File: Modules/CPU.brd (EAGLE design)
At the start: 132.1 x 55.5 mm, 89 parts, among them IC4 93LC66SM, IC5 MIC2026-1YM, J1 USB_A_SMT_FEMALE, J2 USB_A_SMT_FEMALE, J4 SD_CARD_SOCKET, Q1 DMG1012T-7, Q2 DMG1012T-7, Q3 DMG1012T-7, U5 LAN9512-JZX, U6 FSUSB42UMX, Y2 25MHz

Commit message: Added Connectors and Molex
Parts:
- added C1, C2: 0.1uF, SparkFun-Capacitors:0402
- added IC8: AP2331W-7, SamacSys_Parts:SOT95P285X130-3N
- moved R1 67.6 mm to (148.6, 14.0)
- moved PWR_LED 67.6 mm to (144.8, 14.0)
- moved CAM1 56.4 mm to (86.4, 52.1), turned to 180 degrees
- moved SJ4 41.5 mm to (81.3, 41.9)
- moved SJ5 41.0 mm to (74.9, 40.6)
- moved SJ3 39.9 mm to (81.3, 36.8)
- moved CPU1 6.35 mm to (87.6, 8.89)
- moved R22 5.08 mm to (64.0, 17.7)
- moved R23 5.08 mm to (65.4, 17.7)
- moved R24 5.08 mm to (83.7, 17.9)
- moved R25 5.08 mm to (85.1, 17.9)
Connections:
- new net H5V: C2.1, IC8.2
- net 5V: now also C1.2, IC8.3
- net GND: now also C1.1, C2.2, IC8.1
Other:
- board size 132.1 x 55.5 mm -> 132.1 x 55.9 mm

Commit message: Merged HDMI
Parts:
- added IC1: ESD5384NCTBG, SamacSys_Parts:BGA9C40P3X3_114X114X63
- added Q4, Q5: DMG1012T-7, SamacSys_Parts:SOT50P160X80-3N
- added R2: 100K, SparkFun-Resistors:0402
- added U$6: HDMI-A, connectors:HDMI_A
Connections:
- new net HDMI_CEC: CPU1.171, Q4.2
- new net HDMI_CK_N: CPU1.111, U$6.P$12
- new net HDMI_CK_P: CPU1.113, U$6.P$10
- new net HDMI_D0_N: CPU1.117, U$6.P$9
- new net HDMI_D0_P: CPU1.119, U$6.P$7
- new net HDMI_D1_N: CPU1.123, U$6.P$6
- new net HDMI_D1_P: CPU1.125, U$6.P$4
- new net HDMI_D2_N: CPU1.129, U$6.P$3
- new net HDMI_D2_P: CPU1.131, U$6.P$1
- new net HDMI_HPD_N_1V8: CPU1.88, Q5.3, R2.2
- new net HDMI_SCL: CPU1.175, IC1.B3, U$6.P$16
- new net HDMI_SDA: CPU1.173, IC1.A3, U$6.P$15
- new net N$6: IC1.C3, Q5.1, U$6.P$19
- new net N$9: IC1.A2, Q4.3, U$6.P$13
- net 1.8V: now also R2.1
- net GND: now also IC1.B2, IC1.C2, Q5.2, U$6.P$11, U$6.P$17, U$6.P$2, U$6.P$5, U$6.P$8
- net H5V: now also IC1.A1, IC1.C1, Q4.1, U$6.P$18

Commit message: Work
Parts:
- added SJ10: (no value), jumper:SJ
- moved Q4 172.3 mm to (67.3, 44.5)
- moved R2 165.6 mm to (57.1, 43.2)
- moved Q5 165.4 mm to (61.0, 39.4)
- moved IC1 162.6 mm to (62.2, 44.5)
- moved U$6 160.9 mm to (59.7, 50.8), turned to 180 degrees
- moved C2 154.6 mm to (54.6, 44.5)
- moved C1 151.1 mm to (49.5, 36.8)
- moved IC8 147.8 mm to (49.5, 41.9)
- moved C13 129.8 mm to (38.1, 85.1)
- moved C18 115.6 mm to (14.0, 29.2)
- moved FB1 109.6 mm to (14.0, 34.3)
- moved C12 105.4 mm to (-2.54, 30.5)
- moved C11 87.3 mm to (12.7, 64.8)
- moved C16 87.3 mm to (8.89, 64.8)
- moved C17 87.3 mm to (5.08, 64.8)
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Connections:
- net HDMI_CEC: now also SJ10.2

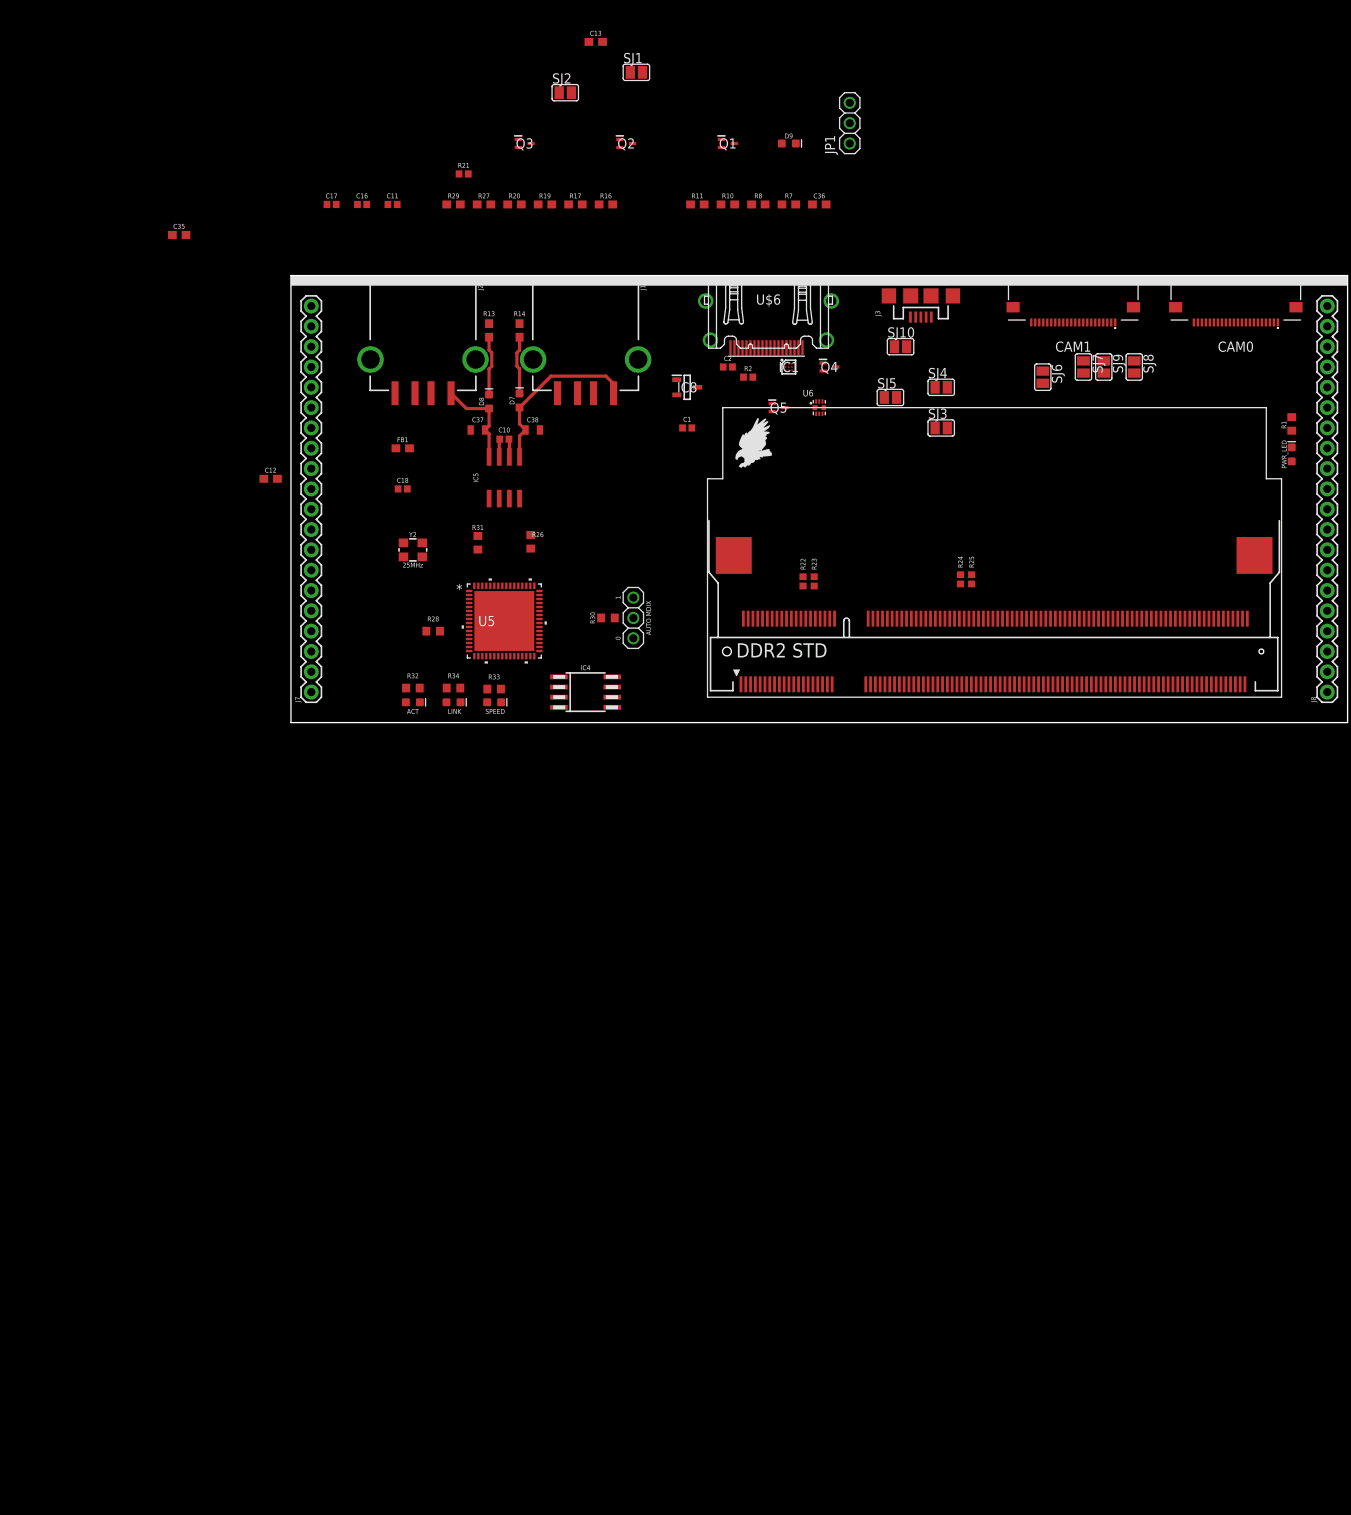
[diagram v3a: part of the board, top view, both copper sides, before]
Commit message: Fixed CAM connectors
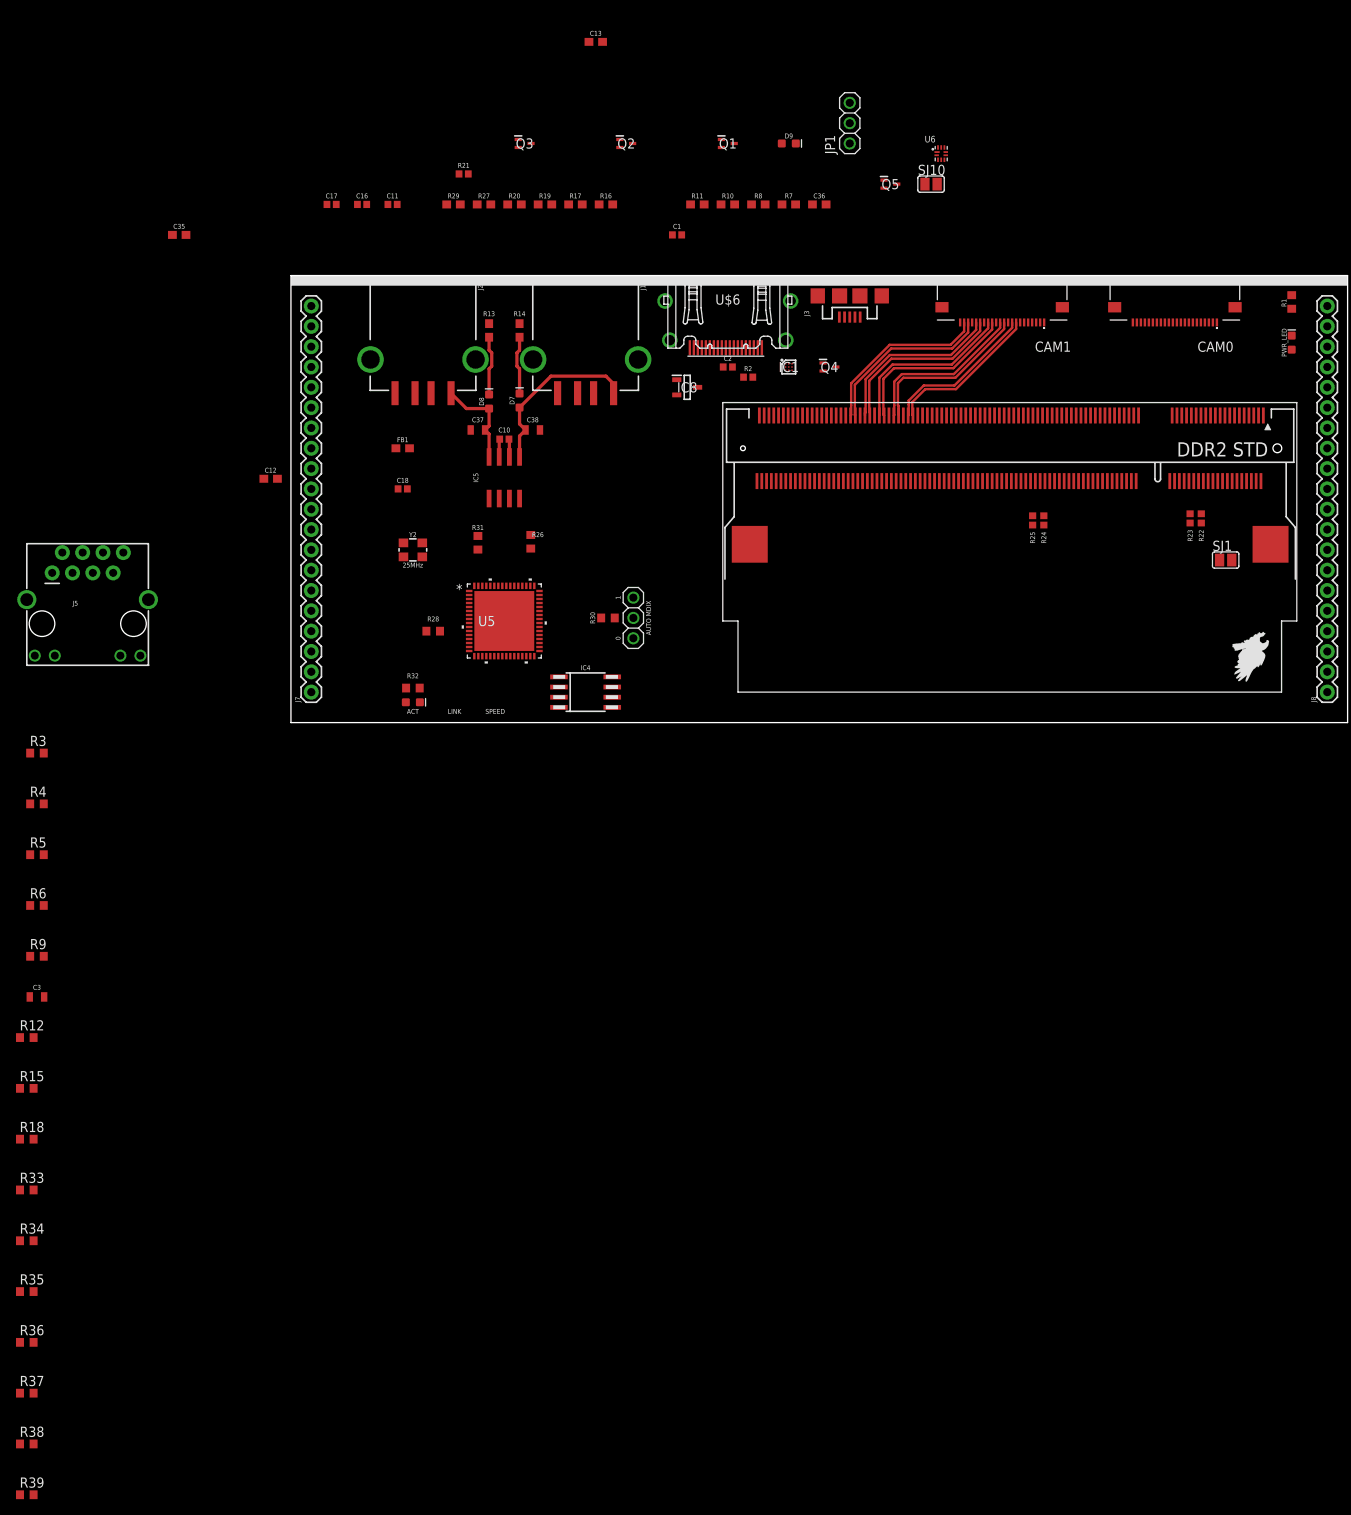
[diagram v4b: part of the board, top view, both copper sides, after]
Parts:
- removed D11_LINK: GREEN, SparkFun-LED:LED-0603
- removed D12_FASTETHER: Yellow, SparkFun-LED:LED-0603
- removed SJ2, SJ3, SJ4, SJ5, SJ6, SJ7, SJ8, SJ9: (no value), jumper:SJ
- added C3: 0.022uF/50V, SparkFun-Capacitors:0805
- added J5: MAGJACK, SparkFun-Connectors:MAGJACK
- added R12, R15: 332R, adafruit:R0603
- added R18, R35, R37, R38: 0R, adafruit:R0603
- added R3, R4, R5, R6: 49.9R, adafruit:R0603
- added R36, R39: 0$, adafruit:R0603
- added R9: 10R, adafruit:R0603
- R33, R34: value 332R -> 0R
- moved SJ1 95.6 mm to (116.8, 20.3)
- moved R34 87.3 mm to (-33.0, -64.8)
- moved R33 85.6 mm to (-33.0, -58.4)
- moved R22 50.4 mm to (113.8, 25.5), turned to 270 degrees
- moved R23 47.6 mm to (112.4, 25.5), turned to 270 degrees
- moved U6 35.2 mm to (81.3, 71.1)
- moved Q5 31.2 mm to (74.9, 67.3)
- moved CPU1 25.5 mm to (90.2, 34.3), turned to 180 degrees
- moved C1 24.2 mm to (48.3, 61.0)
- moved SJ10 20.7 mm to (80.0, 67.3)
- moved R1 15.2 mm to (125.1, 52.6)
- moved PWR_LED 14.0 mm to (125.1, 47.5)
- moved R24 12.8 mm to (94.1, 25.3), turned to 270 degrees
- moved R25 10.6 mm to (92.7, 25.3), turned to 270 degrees
- moved CAM1 8.89 mm to (88.9, 52.1)
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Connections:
- removed net ETH_VDD3A: C19.2, C20.2, C21.2, C22.2, C23.2, C24.2, C25.2, FB2.2, U5.10, U5.49, U5.5, U5.51, U5.54, U5.57, U5.64
- removed net N$25: D12_FASTETHER.C, R33.2
- removed net N$27: D11_LINK.C, R34.2
- removed net N$29: R34.1, U5.21
- removed net N$30: R33.1, U5.22
- new net ETH_VDD33A: C19.2, C20.2, C21.2, C22.2, C23.2, C24.2, C25.2, FB2.2, R3.2, R4.2, R5.2, R6.2, R9.2, U5.10, U5.49, U5.5, U5.51, U5.54, U5.57, U5.64
- new net N$15: J5.12, R15.1
- new net N$3: C3.2, J5.3, J5.6, R9.1
- new net NLNKA: R15.2, U5.21
- new net NSPD: J5.10, R12.1, R12.2, U5.22
- net 3.3V: now also J5.11, J5.9; no longer D11_LINK.A, D12_FASTETHER.A
- net CAM0_IO0: now also R35.2; no longer SJ9.1
- net CAM0_IO1: now also R36.2; no longer SJ8.1
- net CAM0_SCL: now also R37.2; no longer SJ7.1
- net CAM0_SDA: now also R38.2; no longer SJ6.1
- net CAM1_IO0: now also R39.2; no longer SJ5.1
- net CAM1_IO1: now also R34.2; no longer SJ4.1
- net CAM1_SCL: now also R33.2; no longer SJ3.1
- net CAM1_SDA: now also R18.2; no longer SJ2.1
- net GND: now also C3.1, J5.M1, J5.M2
- net GPIO0: now also R18.1; no longer SJ2.2
- net GPIO1: now also R33.1; no longer SJ3.2
- net GPIO28: now also R38.1; no longer SJ6.2
- net GPIO29: now also R37.1; no longer SJ7.2
- net GPIO30: now also R36.1; no longer SJ8.2
- net GPIO31: now also R35.1; no longer SJ9.2
- net GPIO4: now also R34.1; no longer SJ4.2
- net GPIO5: now also R39.1; no longer SJ5.2
- net RX_N: now also J5.2, R6.1
- net RX_P: now also J5.1, R5.1
- net TX_N: now also J5.8, R4.1
- net TX_P: now also J5.7, R3.1
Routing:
- net CAM1_D0_P: track 0.00 -> 22.0 mm
- net CAM1_D0_N: track 0.00 -> 22.0 mm
- net CAM1_D1_N: track 0.00 -> 21.9 mm
- net CAM1_C_P: track 0.00 -> 21.6 mm
- net CAM1_C_N: track 0.00 -> 21.6 mm
- net CAM1_D1_P: track 0.00 -> 21.5 mm
- net CAM1_D2_P: track 0.00 -> 21.0 mm
- net CAM1_D2_N: track 0.00 -> 20.9 mm
- net CAM1_D3_P: track 0.00 -> 19.3 mm
- net CAM1_D3_N: track 0.00 -> 19.3 mm

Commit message: Got a lot of routing done
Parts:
- removed R18, R33, R34, R35, R37, R38: 0R, adafruit:R0603
- removed R36, R39: 0$, adafruit:R0603
- removed SJ10: (no value), jumper:SJ
- moved C21 160.0 mm to (68.6, 21.6), flipped to the top
- moved C22 157.8 mm to (70.0, 21.6), flipped to the top
- moved C20 155.6 mm to (71.4, 21.6), flipped to the top
- moved J4 154.1 mm to (81.3, -29.2), turned to 270 degrees
- moved C19 153.3 mm to (72.8, 21.6), flipped to the top
- moved C25 151.1 mm to (74.2, 21.6), flipped to the top
- moved C24 149.0 mm to (75.6, 21.6), flipped to the top
- moved C23 146.8 mm to (77.0, 21.6), flipped to the top
- moved FB2 144.5 mm to (78.5, 21.5), flipped to the top
- moved C31 132.9 mm to (86.4, 14.0), flipped to the top
- moved C34 131.1 mm to (87.6, 8.89), flipped to the top
- moved C30 130.9 mm to (87.8, 14.0), flipped to the top
- moved C33 129.2 mm to (89.0, 8.89), flipped to the top
- moved C29 129.0 mm to (89.2, 14.0), flipped to the top
- moved C32 127.3 mm to (90.4, 8.89), flipped to the top
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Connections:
- net CM0_D0_P renamed CAM0_D0_P
- removed net CAM0_IO0: CAM0.17, R35.2
- removed net CAM0_IO1: CAM0.18, R36.2
- removed net CAM0_SCL: CAM0.20, R37.2
- removed net CAM0_SDA: CAM0.21, R38.2
- removed net CAM1_IO0: CAM1.17, R39.2
- removed net CAM1_IO1: CAM1.18, R34.2
- removed net CAM1_SCL: CAM1.20, R33.2
- removed net CAM1_SDA: CAM1.21, R18.2
- new net N$12: J5.10, R12.1
- net GPIO0: now also CAM1.21; no longer R18.1
- net GPIO1: now also CAM1.20; no longer R33.1
- net GPIO28: now also CAM0.21; no longer R38.1
- net GPIO29: now also CAM0.20; no longer R37.1
- net GPIO30: now also CAM0.18; no longer R36.1
- net GPIO31: now also CAM0.17; no longer R35.1
- net GPIO4: now also CAM1.18; no longer R34.1
- net GPIO5: now also CAM1.17; no longer R39.1
- net HDMI_CEC: no longer SJ10.2
- net NSPD: no longer J5.10, R12.1
- net RX_N: no longer J7.8
- net RX_P: no longer J7.9
- net TX_N: no longer J7.4
- net TX_P: no longer J7.5
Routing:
- net SCL1: track 0.00 -> 123.8 mm, vias 0 -> 1
- net SDA1: track 0.00 -> 122.5 mm, vias 0 -> 1
- net EMMC_DISABLE_N: track 0.00 -> 81.4 mm, vias 0 -> 2
- net CAM0_D0_P: track 0.00 -> 78.6 mm
- net CAM0_D0_N: track 0.00 -> 75.6 mm
- net GPIO1: track 0.00 -> 54.5 mm, vias 0 -> 2
- net GPIO0: track 0.00 -> 53.1 mm, vias 0 -> 2
- net HDMI_CEC: track 0.00 -> 51.9 mm
- net EMMC_EN_N_1V8: track 0.00 -> 51.8 mm, vias 0 -> 2
- net CAM0_D1_N: track 0.00 -> 51.6 mm
- net CAM0_D1_P: track 0.00 -> 51.6 mm
- net CAM0_C_N: track 0.00 -> 51.5 mm
- net CAM0_C_P: track 0.00 -> 51.4 mm
- net GPIO4: track 0.00 -> 51.2 mm, vias 0 -> 2
- net GPIO5: track 0.00 -> 51.1 mm, vias 0 -> 2
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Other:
- board text removed: "LINK"
- board text removed: "SPEED"

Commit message: More routing
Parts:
- removed C12: 4.7uF, SparkFun-Capacitors:0603
- removed J4: SD_CARD_SOCKET, SparkFun-Connectors:SD
- added C4: 4.7uF, SparkFun-Capacitors:0603
- added J6: 503182-1853, 503182-1853:MOLEX_503182-1853
- moved C16 73.7 mm to (85.0, 14.0), turned to 270 degrees
- moved C11 69.0 mm to (83.6, 14.0), turned to 90 degrees
- moved C1 54.8 mm to (63.5, 21.6), turned to 90 degrees
- moved C32 41.6 mm to (49.8, 17.8)
- moved C33 41.6 mm to (48.4, 17.8)
- moved C34 41.6 mm to (47.0, 17.8)
- moved FB1 5.06 mm to (34.2, 14.2)
- moved R32 3.27 mm to (46.3, 23.2), turned to 45 degrees
- moved R12 2.54 mm to (5.08, 5.41)
- moved D10-FULLDUPLEX 2.38 mm to (49.9, 23.9), turned to 180 degrees
- moved SJ1 1.37 mm to (118.1, 22.1)
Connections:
- net ETH_USBDM renamed ETH_USBD_N
- net ETH_USBDP renamed ETH_USBD_P
- net ETH_USB_DM2 renamed ETH_USB_D2_N
- net ETH_USB_DM3 renamed ETH_USB_D3_N
- net ETH_USB_DP2 renamed ETH_USB_D2_P
- net ETH_USB_DP3 renamed ETH_USB_D3_P
- net 3.3V: now also C4.1, J6.4; no longer C12.1, J4.4
- net GND: now also C4.2, J6.6, J6.SH1, J6.SH2, J6.SH3, J6.SH4, J6.SH5; no longer C12.2, J4.3, J4.6, J4.SH@1, J4.SH@2
- net SD_CLK: now also J6.5; no longer J4.5
- net SD_CMD: now also J6.3; no longer J4.2
- net SD_D0: now also J6.7; no longer J4.7
- net SD_D1: now also J6.8; no longer J4.8
- net SD_D2: now also J6.1; no longer J4.9
- net SD_D3: now also J6.2; no longer J4.1
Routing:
- net 3.3V: track 0.00 -> 153.4 mm, vias 0 -> 9
- net ETH_USB_D2_P: track 0.00 -> 82.3 mm
- net ETH_USB_D2_N: track 0.00 -> 81.3 mm
- net 1.8V: track 0.00 -> 58.5 mm, vias 0 -> 3
- net 5V: track 2.25 -> 60.2 mm, vias 0 -> 5
- net ETH_USBD_N: track 0.00 -> 53.1 mm, vias 0 -> 4
- net ETH_USB_D3_N: track 0.00 -> 51.6 mm
- net ETH_USBD_P: track 0.00 -> 51.6 mm, vias 0 -> 4
- net NSPD: track 0.00 -> 51.3 mm, vias 0 -> 2
- net ETH_USB_D3_P: track 0.00 -> 50.8 mm
- net N$10: track 1.27 -> 50.8 mm, vias 0 -> 2
- net N$11: track 1.27 -> 39.6 mm, vias 0 -> 2
- net NLNKA: track 0.00 -> 37.0 mm, vias 0 -> 2
- net ETH_VDD18CORE: track 0.00 -> 33.2 mm, vias 0 -> 4
- net SD_D1: track 0.00 -> 20.2 mm, vias 0 -> 1
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- added copper zone on layer 1, net GND
- added copper zone on layer 16, net GND

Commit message: more routing
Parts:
- added U$1: (no value), SparkFun-Aesthetics:OSHW-LOGO-L
- moved R31 0.33 mm to (39.5, 12.4)
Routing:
- net 3.3V: track 153.4 -> 369.4 mm, vias 9 -> 26
- net ETH_VDD33A: track 9.97 -> 90.1 mm, vias 0 -> 7
- net 1.8V: track 58.5 -> 123.4 mm, vias 3 -> 8
- net 5V: track 60.2 -> 121.1 mm, vias 5 -> 8
- net N$10: track 50.8 -> 53.6 mm
- net ETH_USB_D2_P: track 82.3 -> 85.1 mm
- net GPIO0: track 53.1 -> 55.4 mm
- net ETH_USB_D2_N: track 81.3 -> 83.5 mm
- net ETH_USB_D3_N: track 51.6 -> 53.2 mm
- net ETH_USB_D3_P: track 50.8 -> 52.1 mm
- net SPI1_SCLK: track 37.1 -> 38.3 mm
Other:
- board text added: "PoolTable CPU REV A Created by DART 2019 Released under the GPLv3"
